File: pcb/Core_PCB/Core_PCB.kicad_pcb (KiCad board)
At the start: 2 copper layers, 85 x 100 mm, 63 parts, among them J1 Conn_01x02_MountingPin, J10 Conn_01x12, J2 Conn_01x02_MountingPin, J3 Conn_01x02_MountingPin, J4 Conn_01x04_MountingPin, J5 Conn_01x06, J6 Screw_Terminal_01x02, J7 Conn_01x02_MountingPin, J8 Conn_01x08, J9 Conn_01x08, Q1 BSN20, SW1 SW_Push, SW2 SW_Push, SW3 SW_Push, U1 MAX98357A, U2 HEF4051BT, U3 MPR121_BREAKOUT, U4 MCP23017x-x-SS

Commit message: PCB - initial layout
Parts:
- moved RV1 84.8 mm to (181.5, 87.9), turned to 180 degrees
- moved C8 80.0 mm to (176.5, 83.0), turned to 0 degrees
- moved R3 78.3 mm to (176.5, 84.6), turned to 180 degrees
- moved J3 22.9 mm to (105.7, 80.5)
- moved J4 12.6 mm to (105.7, 69.4)
- moved C3 12.4 mm to (116.9, 57.2), turned to -90 degrees
- moved J2 12.0 mm to (104.8, 57.5)
- moved R5 8.88 mm to (112.0, 133.5), turned to 180 degrees
- moved SW1 8.32 mm to (148.8, 120.1), turned to -90 degrees
- moved R6 8.17 mm to (115.0, 135.0), turned to 0 degrees
- moved R7 7.19 mm to (116.5, 133.5), turned to 180 degrees
- moved C9 6.52 mm to (112.0, 136.5), turned to 180 degrees
- moved C24 6.37 mm to (142.0, 138.0), turned to 0 degrees
- moved R8 6.36 mm to (119.5, 135.0), turned to 0 degrees
- moved C10 6.33 mm to (115.0, 138.0), turned to 0 degrees
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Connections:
- net VCC renamed +5V
- A1 pad A6: /display/RTC_SQW -> unconnected-(A1-PadA6)
- A1 pad D2: /display/DISPLAY_CLK -> /display/RTC_SQW
- A1 pad D4: unconnected-(A1-PadD4) -> /display/DISPLAY_CLK
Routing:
- net +3V3: track 0.00 -> 329.3 mm, vias 0 -> 1
- net +5V: track 0.00 -> 192.0 mm, vias 0 -> 2
- net /buttons/SCL: track 0.00 -> 138.2 mm, vias 0 -> 2
- net /buttons/SDA: track 0.00 -> 137.0 mm, vias 0 -> 3
- net GND: track 0.00 -> 116.7 mm, vias 0 -> 107
- net /processor/SDCARD_SCK: track 0.00 -> 43.3 mm
- net /audio/GAIN_MUX_S3: track 0.00 -> 41.1 mm, vias 0 -> 1
- net /audio/GAIN_MUX_S1: track 0.00 -> 37.8 mm, vias 0 -> 1
- net /audio/GAIN_MUX_S2: track 0.00 -> 37.8 mm, vias 0 -> 1
- net /buttons/BT6: track 0.00 -> 34.9 mm
- net /buttons/VOLUME_POT: track 0.00 -> 33.0 mm, vias 0 -> 1
- net /buttons/BT5: track 0.00 -> 32.8 mm
- net /buttons/AFC: track 0.00 -> 30.1 mm
- net /buttons/BT4: track 0.00 -> 29.7 mm
- net /buttons/OFF: track 0.00 -> 29.6 mm
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- added copper zone on B.Cu, net GND
- added copper zone on F.Cu, net GND

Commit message: moved sch changes to PCB, screws placement is not definitive
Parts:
- removed RV1: 100k, Connector_PinSocket_2.54mm:PinSocket_1x03_P2.54mm_Vertical
- added H1: MountingScrew, MountingHole:MountingHole_3.2mm_M3, F.Cu at (105.0, 125.0)
- added H2: MountingScrew, MountingHole:MountingHole_3.2mm_M3, F.Cu at (148.0, 135.0)
- added H3: MountingScrew, MountingHole:MountingHole_3.2mm_M3, F.Cu at (180.0, 55.0)
- added H4: MountingScrew, MountingHole:MountingHole_3.2mm_M3, F.Cu at (140.0, 55.0)
- added J11: Conn_01x03_MountingPin, Connector_Molex:Molex_PicoBlade_53261-0371_1x03-1MP_P1.25mm_Horizontal, F.Cu at (180.2, 92.0)
- added LF1: ~, RadioWecker:LEAF, F.Cu at (155.9, 54.4)
- J10: value Conn_01x12 -> Conn_02x12_Odd_Even; footprint Connector_PinSocket_2.54mm:PinSocket_1x12_P2.54mm_Vertical -> Connector_PinSocket_2.54mm:PinSocket_2x12_P2.54mm_Vertical
- moved C8 10.2 mm to (169.5, 90.4)
- moved R3 10.2 mm to (169.5, 92.0)
- moved J10 2.50 mm to (153.5, 144.7)
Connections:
- net +5V renamed VCC
- net /buttons/VOLUME_POT renamed /audio/VOLUME_POT
- J10 pad 10: Net-(J10-Pin_10) -> GND
- J10 pad 12: Net-(J10-Pin_12) -> GND
- J10 pad 2: Net-(J10-Pin_2) -> GND
- J10 pad 4: Net-(J10-Pin_4) -> GND
- J10 pad 6: Net-(J10-Pin_6) -> GND
- J10 pad 8: Net-(J10-Pin_8) -> GND
- U3 pad 10: Net-(J10-Pin_4) -> Net-(J10-Pin_7)
- U3 pad 11: Net-(J10-Pin_5) -> Net-(J10-Pin_9)
- U3 pad 12: Net-(J10-Pin_6) -> Net-(J10-Pin_11)
- U3 pad 13: Net-(J10-Pin_7) -> Net-(J10-Pin_13)
- U3 pad 14: Net-(J10-Pin_8) -> Net-(J10-Pin_15)
- U3 pad 15: Net-(J10-Pin_9) -> Net-(J10-Pin_17)
- U3 pad 16: Net-(J10-Pin_10) -> Net-(J10-Pin_19)
- U3 pad 17: Net-(J10-Pin_11) -> Net-(J10-Pin_21)
- U3 pad 18: Net-(J10-Pin_12) -> Net-(J10-Pin_23)
- U3 pad 8: Net-(J10-Pin_2) -> Net-(J10-Pin_3)
- U3 pad 9: Net-(J10-Pin_3) -> Net-(J10-Pin_5)
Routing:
- net GND: track 116.7 -> 164.7 mm, vias 107 -> 106
- net Net-(J10-Pin_8): track 8.94 -> 0.00 mm
- net Net-(J10-Pin_6): track 8.94 -> 0.00 mm
- net Net-(J10-Pin_4): track 8.94 -> 0.00 mm
- net Net-(J10-Pin_2): track 8.94 -> 0.00 mm
- net Net-(J10-Pin_12): track 8.94 -> 0.00 mm
- net Net-(J10-Pin_10): track 8.94 -> 0.00 mm
- net Net-(J10-Pin_21): track 0.00 -> 6.48 mm
- net Net-(J10-Pin_17): track 0.00 -> 6.48 mm
- net Net-(J10-Pin_13): track 0.00 -> 6.48 mm
- net Net-(J10-Pin_23): track 0.00 -> 6.44 mm
- net Net-(J10-Pin_19): track 0.00 -> 6.44 mm
- net Net-(J10-Pin_15): track 0.00 -> 6.44 mm
- net Net-(J11-Pin_2): track 4.39 -> 7.39 mm
- net Net-(J10-Pin_7): track 8.94 -> 6.44 mm
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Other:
- board text added: "32K"
- board text added: "5V"
- board text added: "BT0"
- board text added: "BT1"
- board text added: "BT2"
- board text added: "BT3"
- board text added: "BT4"
- board text added: "BT5"
- board text added: "BT6"
- board text added: "CLK"
- board text added: "CS"
- board text added: "DIO"
- board text added: "GND"
- board text added: "MISO"
- board text added: "MOSI"
- board text added: "PWM"
- board text added: "SCK"
- board text added: "SCL"
- board text added: "SDA"
- board text added: "SQW"
- board text added: "WIPER"

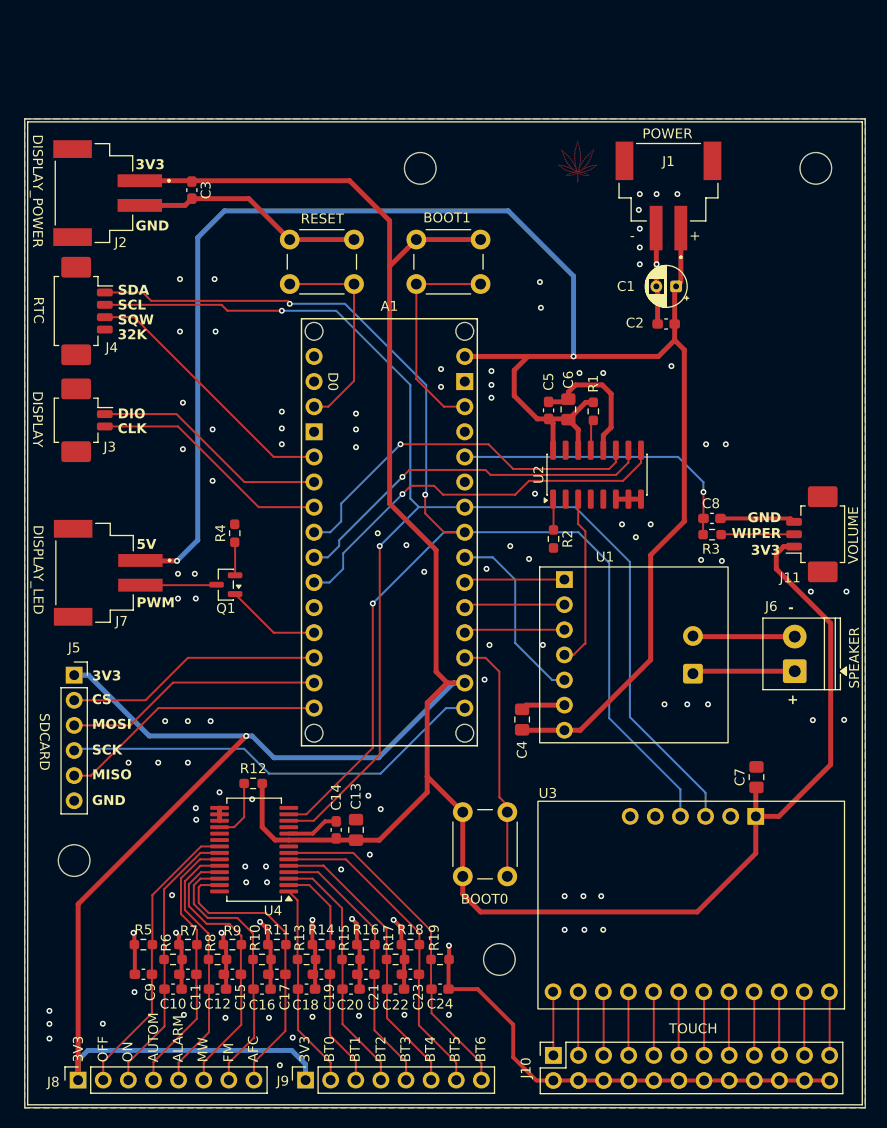
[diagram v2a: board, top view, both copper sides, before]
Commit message: PCB: adjusted size and screws positions to correct values, new component positions, new layout and bumped the date
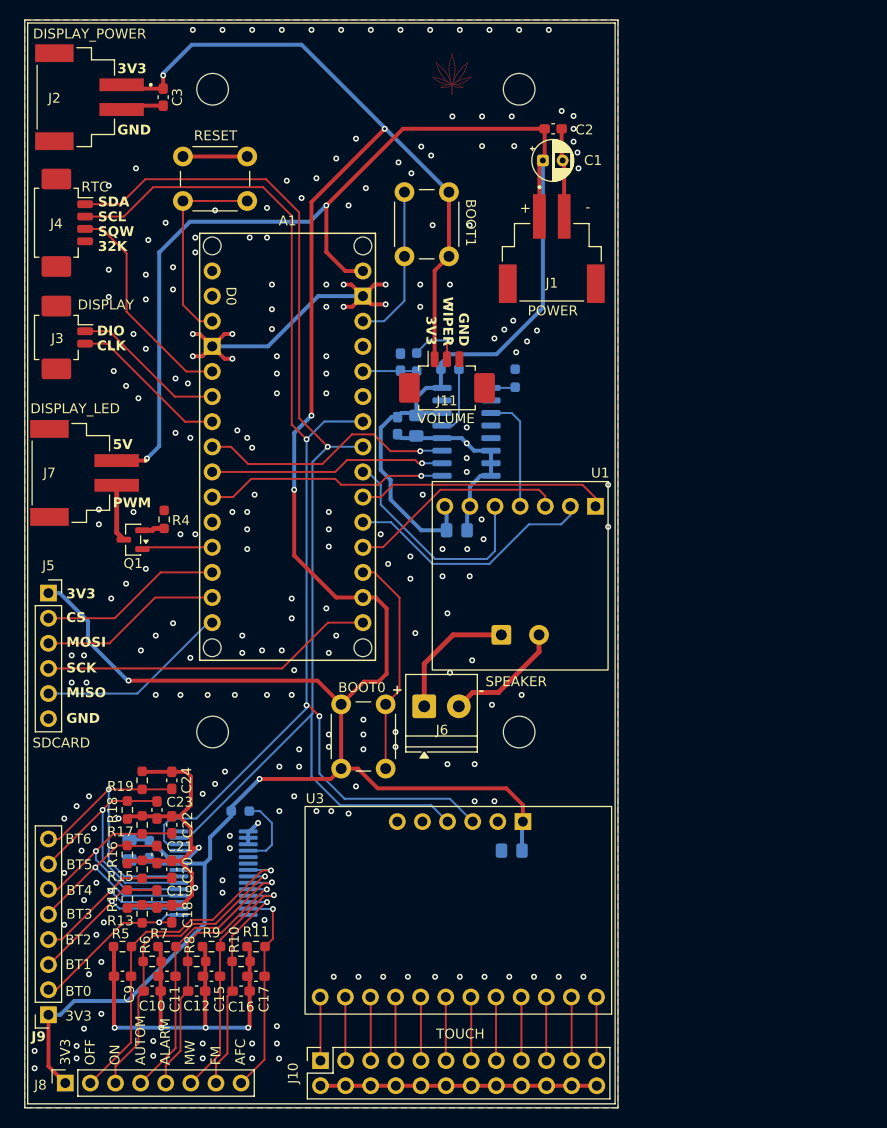
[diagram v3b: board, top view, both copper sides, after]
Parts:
- C13, C14, C4, C5, C6, C7, C8, R1, R12, R2, R3, U2, U4: moved to B.Cu
- moved J11 40.5 mm to (142.7, 76.7), turned to 0 degrees
- moved J6 37.6 mm to (140.4, 109.4), turned to 0 degrees
- moved C8 35.2 mm to (138.0, 74.6), turned to 90 degrees
- moved R19 35.2 mm to (111.9, 116.9), turned to 90 degrees
- moved R3 34.6 mm to (139.6, 74.6), turned to -90 degrees
- moved C24 34.4 mm to (114.9, 116.9), turned to 90 degrees
- moved R18 31.7 mm to (110.4, 119.9), turned to -90 degrees
- moved H3 31.0 mm to (150.0, 47.0)
- moved C23 30.5 mm to (113.4, 119.9), turned to -90 degrees
- moved R17 29.0 mm to (111.9, 121.4), turned to 90 degrees
- moved U1 28.6 mm to (141.2, 86.7), turned to -90 degrees
- moved C22 28.1 mm to (114.9, 121.4), turned to 90 degrees
- moved J9 26.8 mm to (102.4, 140.6), turned to 180 degrees
- moved C7 25.8 mm to (149.2, 124.0), turned to 180 degrees
- moved R16 25.8 mm to (110.4, 124.4), turned to -90 degrees
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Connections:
- net VCC renamed +5V
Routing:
- net +3V3: track 327.6 -> 257.9 mm, vias 1 -> 6
- net +5V: track 192.0 -> 145.8 mm
- net GND: track 164.7 -> 202.8 mm, vias 106 -> 233
- net /audio/VOLUME_POT: track 30.8 -> 5.46 mm, vias 2 -> 0
- net /audio/GAIN_MUX_S3: track 41.1 -> 24.6 mm
- net /buttons/SDA: track 137.0 -> 120.8 mm, vias 3 -> 1
- net /audio/BCLK: track 10.2 -> 25.7 mm
- net /audio/LRCLK: track 10.2 -> 25.4 mm
- net /audio/GAIN_MUX_S2: track 37.8 -> 23.9 mm
- net /audio/DIN: track 10.2 -> 22.2 mm
- net /audio/GAIN_MUX_S1: track 37.8 -> 25.9 mm
- net /buttons/SCL: track 138.2 -> 127.8 mm, vias 2 -> 3
- net /processor/SDCARD_SCK: track 43.3 -> 33.7 mm
- net /buttons/AFC: track 30.1 -> 21.5 mm, vias 0 -> 1
- net /display/DISPLAY_CLK: track 24.5 -> 16.1 mm
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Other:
- board size 85 x 100 mm -> 60 x 110 mm
